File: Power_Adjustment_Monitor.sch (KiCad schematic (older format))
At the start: 15 parts, among them U10 LM7805, U11 LM317, U8 LM317, U9 LM7805

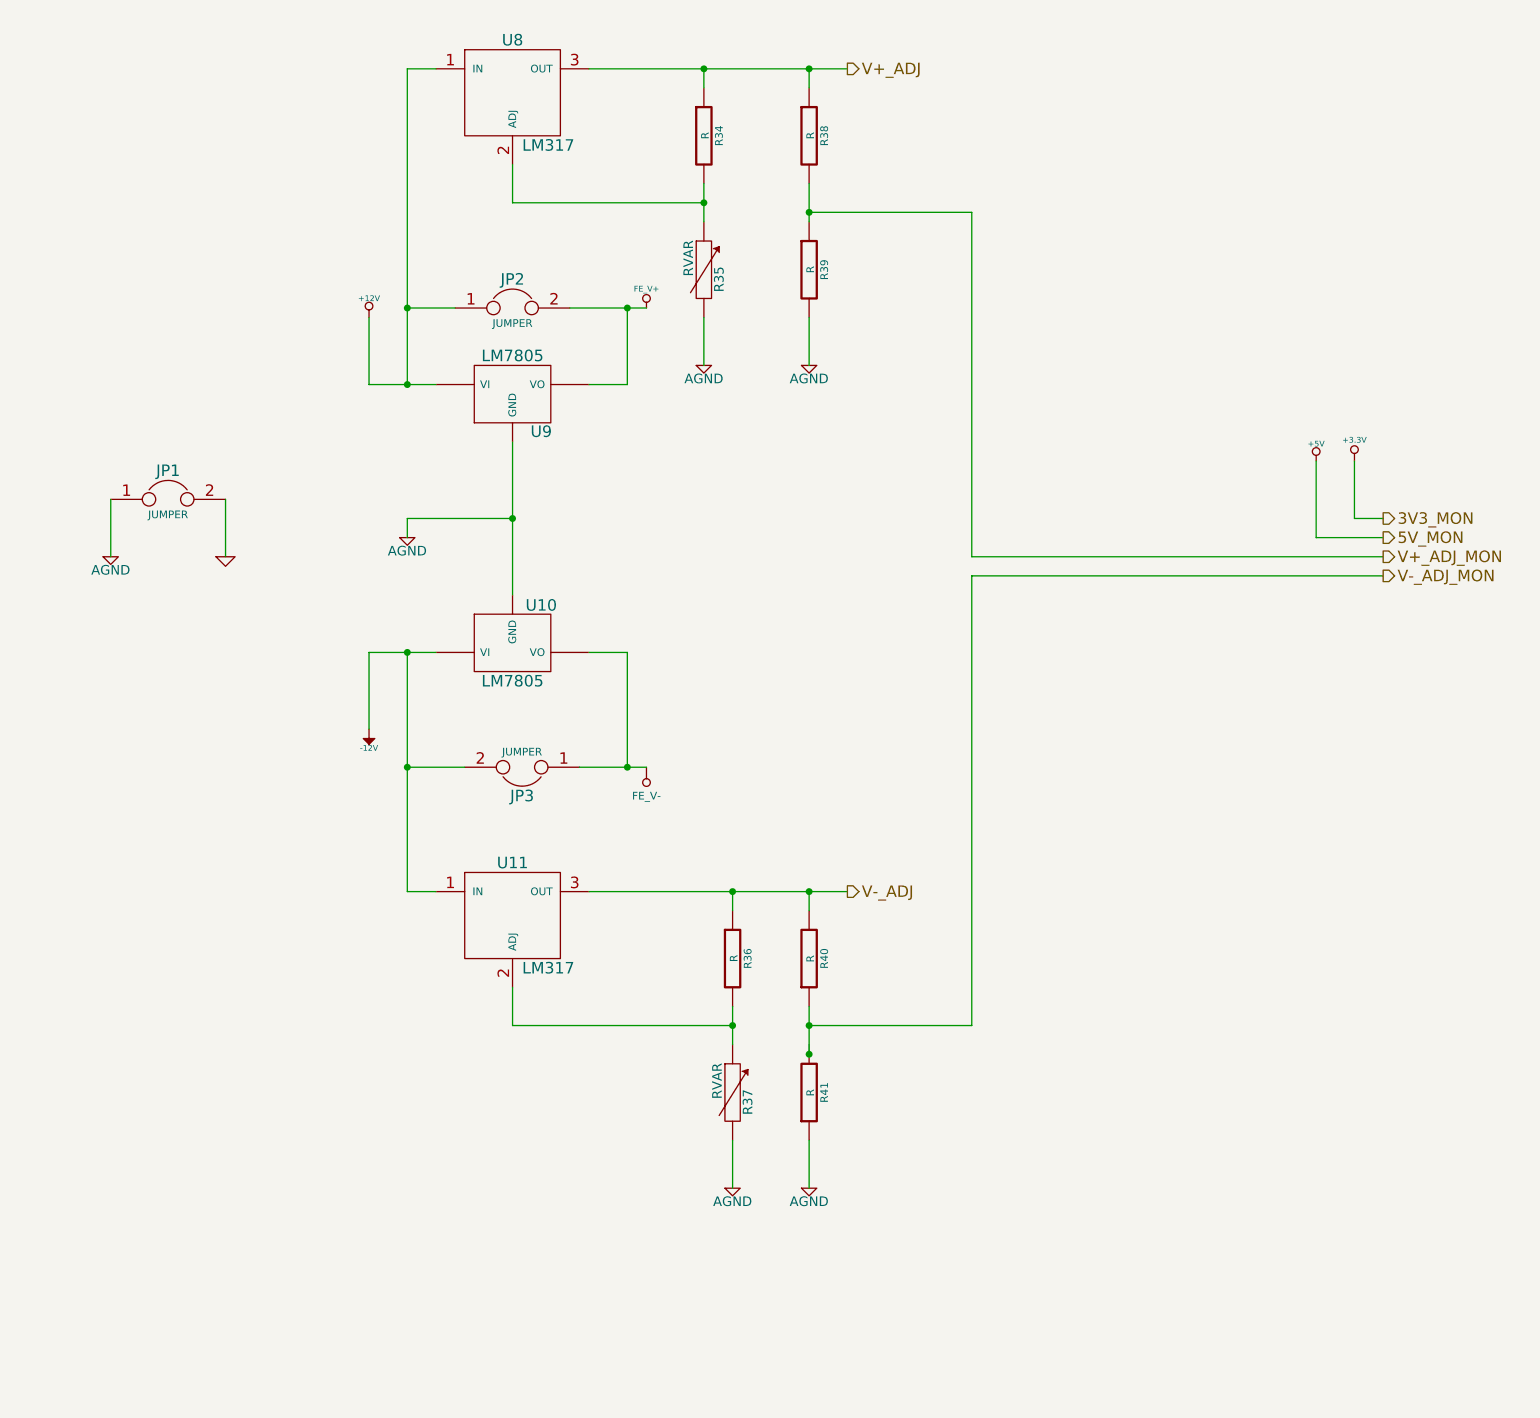
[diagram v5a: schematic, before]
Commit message: Completed placement and association of all footprints
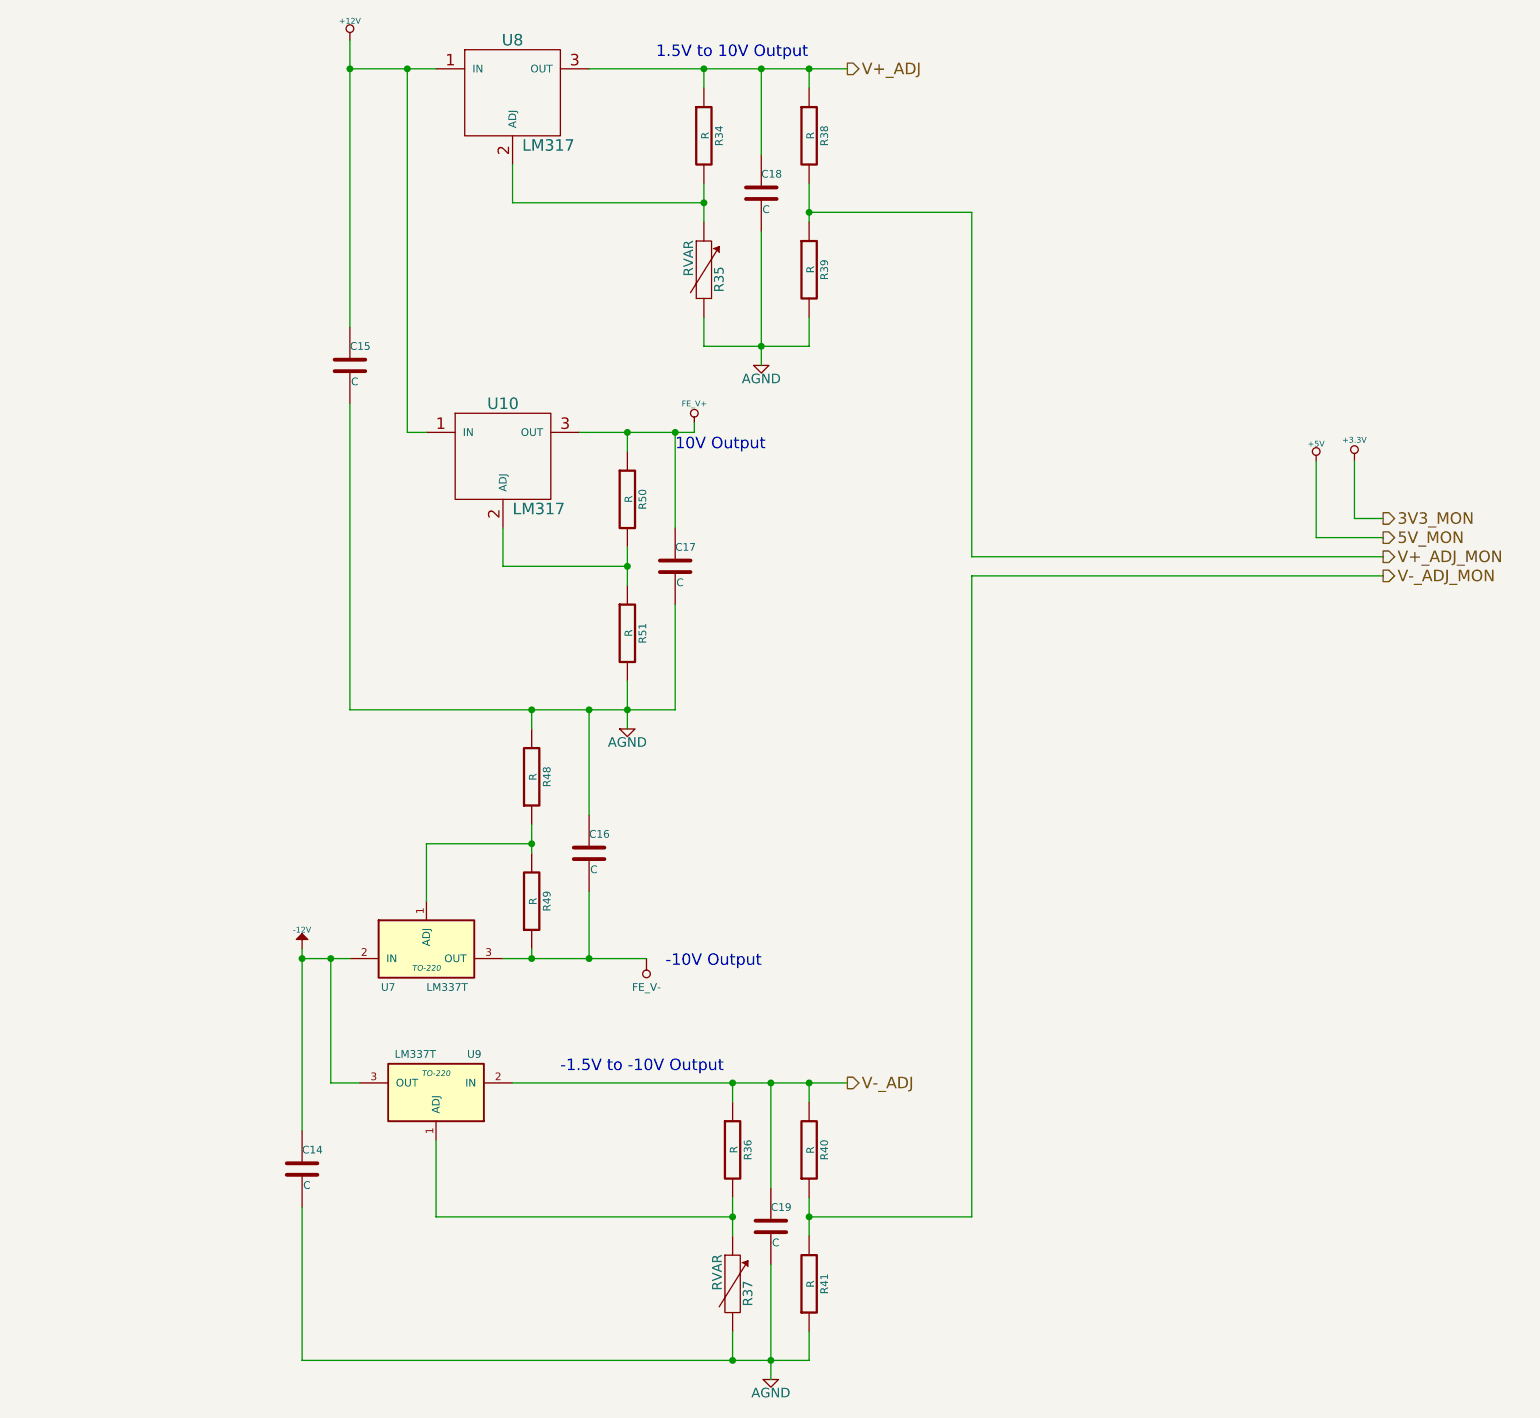
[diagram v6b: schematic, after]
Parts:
- removed JP1, JP2, JP3: JUMPER, ~, symbol JUMPER
- removed U10, U9: LM7805, ~, symbol LM7805
- removed U11: LM317, ~, symbol LM317
- added C14, C15, C16, C17, C18, C19: C, ~, symbol C
- added R48, R49, R50, R51: R, ~, symbol R
- added U10: LM317, ~, symbol LM317
- added U7, U9: LM337T, TO-220, symbol LM337T
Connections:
- net +12V: now also C15.1, U10.1 (IN)
- net -12V: now also C14.1, U7.2 (IN), U9.3 (OUT)
- net AGND: now also C14.2, C15.2, C16.1, C17.2, C18.2, C19.2, R48.2, R51.2
- net FE_V+: now also C17.1, R50.1, U10.3 (OUT)
- net FE_V-: now also C16.2, R49.1, U7.3 (OUT)
- net V+_ADJ: now also C18.1
- net V-_ADJ: now also C19.1, U9.2 (IN)
- net V-_ADJ_MON: now also R41.2
- net at R36.2, R37.1: now also U9.1 (ADJ)
- new net: R50.2, R51.1, U10.2 (ADJ)
- new net: R48.1, R49.2, U7.1 (ADJ)
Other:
- note added: "-1.5V to -10V Output"
- note added: "-10V Output"
- note added: "1.5V to 10V Output"
- note added: "10V Output"
- moved on the sheet: R36, R37, R40, R41

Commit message: Layout v1.0
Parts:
- removed U10, U8: LM317, ~, symbol LM317
- added JP1: JUMPER, ~, symbol JUMPER
- added U10, U8: LM317K, TO-220, symbol LM317K
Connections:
- net +12V: now also U10.2 (IN), U8.2 (IN)
- net -12V: now also U9.2 (IN); no longer U9.3 (OUT)
- net AGND: now also JP1.1
- net FE_V+: now also U8.3 (OUT)
- net V+_ADJ: now also U10.3 (OUT)
- net V-_ADJ: now also U9.3 (OUT); no longer U9.2 (IN)
- net at R34.2, R35.1: now also U10.1 (ADJ)
- net at R50.2, R51.1: now also U8.1 (ADJ)
- new net GND: JP1.2
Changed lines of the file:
@@
 Sheet 8 9
 Title ""
-Date "28 feb 2014"
+Date "3 mar 2014"
 Rev ""
 Comp ""
@@
 $EndDescr
 $Comp
-L +3.3V #PWR056
+L +3.3V #PWR052
 U 1 1 52F8235F
 P 8000 2850
-F 0 "#PWR056" H 8000 2810 30  0001 C CNN
+F 0 "#PWR052" H 8000 2810 30  0001 C CNN
 F 1 "+3.3V" H 8000 2960 30  0000 C CNN
 F 2 "" H 8000 2850 60  0000 C CNN
@@
 $EndComp
 $Comp
-L +5V #PWR057
+L +5V #PWR053
 U 1 1 52F82365
 P 7800 2850
-F 0 "#PWR057" H 7800 2940 20  0001 C CNN
+F 0 "#PWR053" H 7800 2940 20  0001 C CNN
 F 1 "+5V" H 7800 2940 30  0000 C CNN
 F 2 "" H 7800 2850 60  0000 C CNN
@@
 $EndComp
 $Comp
-L -12V #PWR058
+L -12V #PWR054
 U 1 1 52F823F0
 P 2500 5400
-F 0 "#PWR058" H 2500 5530 20  0001 C CNN
+F 0 "#PWR054" H 2500 5530 20  0001 C CNN
 F 1 "-12V" H 2500 5500 30  0000 C CNN
 F 2 "" H 2500 5400 60  0000 C CNN
@@
 $EndComp
 $Comp
-L +12V #PWR059
+L +12V #PWR055
 U 1 1 52F823F6
 P 2750 650
-F 0 "#PWR059" H 2750 600 20  0001 C CNN
+F 0 "#PWR055" H 2750 600 20  0001 C CNN
 F 1 "+12V" H 2750 750 30  0000 C CNN
 F 2 "" H 2750 650 60  0000 C CNN
@@
 $EndComp
 $Comp
-L LM317 U8
-U 1 1 52F82C8E
-P 3600 950
-F 0 "U8" H 3600 1250 60  0000 C CNN
-F 1 "LM317" H 3650 700 60  0000 L CNN
-F 2 "~" H 3600 950 60  0000 C CNN
-F 3 "~" H 3600 950 60  0000 C CNN
-	1    3600 950
-	1    0    0    -1
-$EndComp
-$Comp
-L FE_V+ #PWR060
+L FE_V+ #PWR056
 U 1 1 52F8326E
 P 4550 2650
-F 0 "#PWR060" H 4550 2750 30  0001 C CNN
+F 0 "#PWR056" H 4550 2750 30  0001 C CNN
 F 1 "FE_V+" H 4550 2750 30  0000 C CNN
 F 2 "" H 4550 2650 60  0000 C CNN
@@
 $EndComp
 $Comp
-L AGND #PWR061
+L AGND #PWR057
 U 1 1 52F83482
 P 4900 2350
-F 0 "#PWR061" H 4900 2350 40  0001 C CNN
+F 0 "#PWR057" H 4900 2350 40  0001 C CNN
 F 1 "AGND" H 4900 2280 50  0000 C CNN
 F 2 "" H 4900 2350 60  0000 C CNN
@@
 $EndComp
 $Comp
-L AGND #PWR062
+L AGND #PWR058
 U 1 1 52F83839
 P 4950 7650
-F 0 "#PWR062" H 4950 7650 40  0001 C CNN
+F 0 "#PWR058" H 4950 7650 40  0001 C CNN
 F 1 "AGND" H 4950 7580 50  0000 C CNN
 F 2 "" H 4950 7650 60  0000 C CNN
 F 3 "" H 4950 7650 60  0000 C CNN
 	1    4950 7650
-	1    0    0    -1
-$EndComp
-$Comp
-L LM317 U10
-U 1 1 530D992E
-P 3550 2850
-F 0 "U10" H 3550 3150 60  0000 C CNN
-F 1 "LM317" H 3600 2600 60  0000 L CNN
-F 2 "~" H 3550 2850 60  0000 C CNN
-F 3 "~" H 3550 2850 60  0000 C CNN
-	1    3550 2850
 	1    0    0    -1
 $EndComp
@@
 F 3 "~" H 3200 6150 60  0000 C CNN
 	1    3200 6150
-	-1   0    0    1
+	1    0    0    1
 $EndComp
 $Comp
@@
 $EndComp
 $Comp
-L AGND #PWR063
+L AGND #PWR059
 U 1 1 530D993A
 P 4200 4250
-F 0 "#PWR063" H 4200 4250 40  0001 C CNN
+F 0 "#PWR059" H 4200 4250 40  0001 C CNN
 F 1 "AGND" H 4200 4180 50  0000 C CNN
 F 2 "" H 4200 4250 60  0000 C CNN
@@
 Connection ~ 4200 2700
 Wire Wire Line
-	3550 3400 3550 3200
+	3550 3400 3550 3000
 Wire Wire Line
 	4200 4000 4200 4250
@@
 Connection ~ 4600 800
 Wire Wire Line
-	3600 1500 3600 1300
+	3600 1500 3600 1100
 Wire Wire Line
 	4900 1650 4900 2350
@@
 	2750 2550 2750 4150
 Connection ~ 3700 4150
+$Comp
+L AGND #PWR060
+U 1 1 5312E702
+P 1650 3800
+F 0 "#PWR060" H 1650 3800 40  0001 C CNN
+F 1 "AGND" H 1650 3730 50  0000 C CNN
+F 2 "" H 1650 3800 60  0000 C CNN
+F 3 "" H 1650 3800 60  0000 C CNN
+	1    1650 3800
+	1    0    0    -1
+$EndComp
+$Comp
+L GND #PWR061
+U 1 1 5312E70A
+P 1050 3800
+F 0 "#PWR061" H 1050 3800 30  0001 C CNN
+F 1 "GND" H 1050 3730 30  0001 C CNN
+F 2 "" H 1050 3800 60  0000 C CNN
+F 3 "" H 1050 3800 60  0000 C CNN
+	1    1050 3800
+	1    0    0    -1
+$EndComp
+$Comp
+L JUMPER JP1
+U 1 1 5312E719
+P 1350 3400
+F 0 "JP1" H 1350 3550 60  0000 C CNN
+F 1 "JUMPER" H 1350 3320 40  0000 C CNN
+F 2 "~" H 1350 3400 60  0000 C CNN
+F 3 "~" H 1350 3400 60  0000 C CNN
+	1    1350 3400
+	-1   0    0    1
+$EndComp
+Wire Wire Line
+	1650 3400 1650 3800
+Wire Wire Line
+	1050 3400 1050 3800
+$Comp
+L LM317K U10
+U 1 1 53143282
+P 3600 850
+F 0 "U10" H 3400 1050 40  0000 C CNN
+F 1 "LM317K" H 3600 1050 40  0000 L CNN
+F 2 "TO-220" H 3600 950 30  0000 C CIN
+F 3 "~" H 3600 850 60  0000 C CNN
+	1    3600 850
+	1    0    0    -1
+$EndComp
+$Comp
+L LM317K U8
+U 1 1 531432A3
+P 3550 2750
+F 0 "U8" H 3350 2950 40  0000 C CNN
+F 1 "LM317K" H 3550 2950 40  0000 L CNN
+F 2 "TO-220" H 3550 2850 30  0000 C CIN
+F 3 "~" H 3550 2750 60  0000 C CNN
+	1    3550 2750
+	1    0    0    -1
+$EndComp
 $EndSCHEMATC
